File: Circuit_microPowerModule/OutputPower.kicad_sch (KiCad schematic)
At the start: 31 parts, among them U4 LM358, U7 MP2315S, U8 LM358

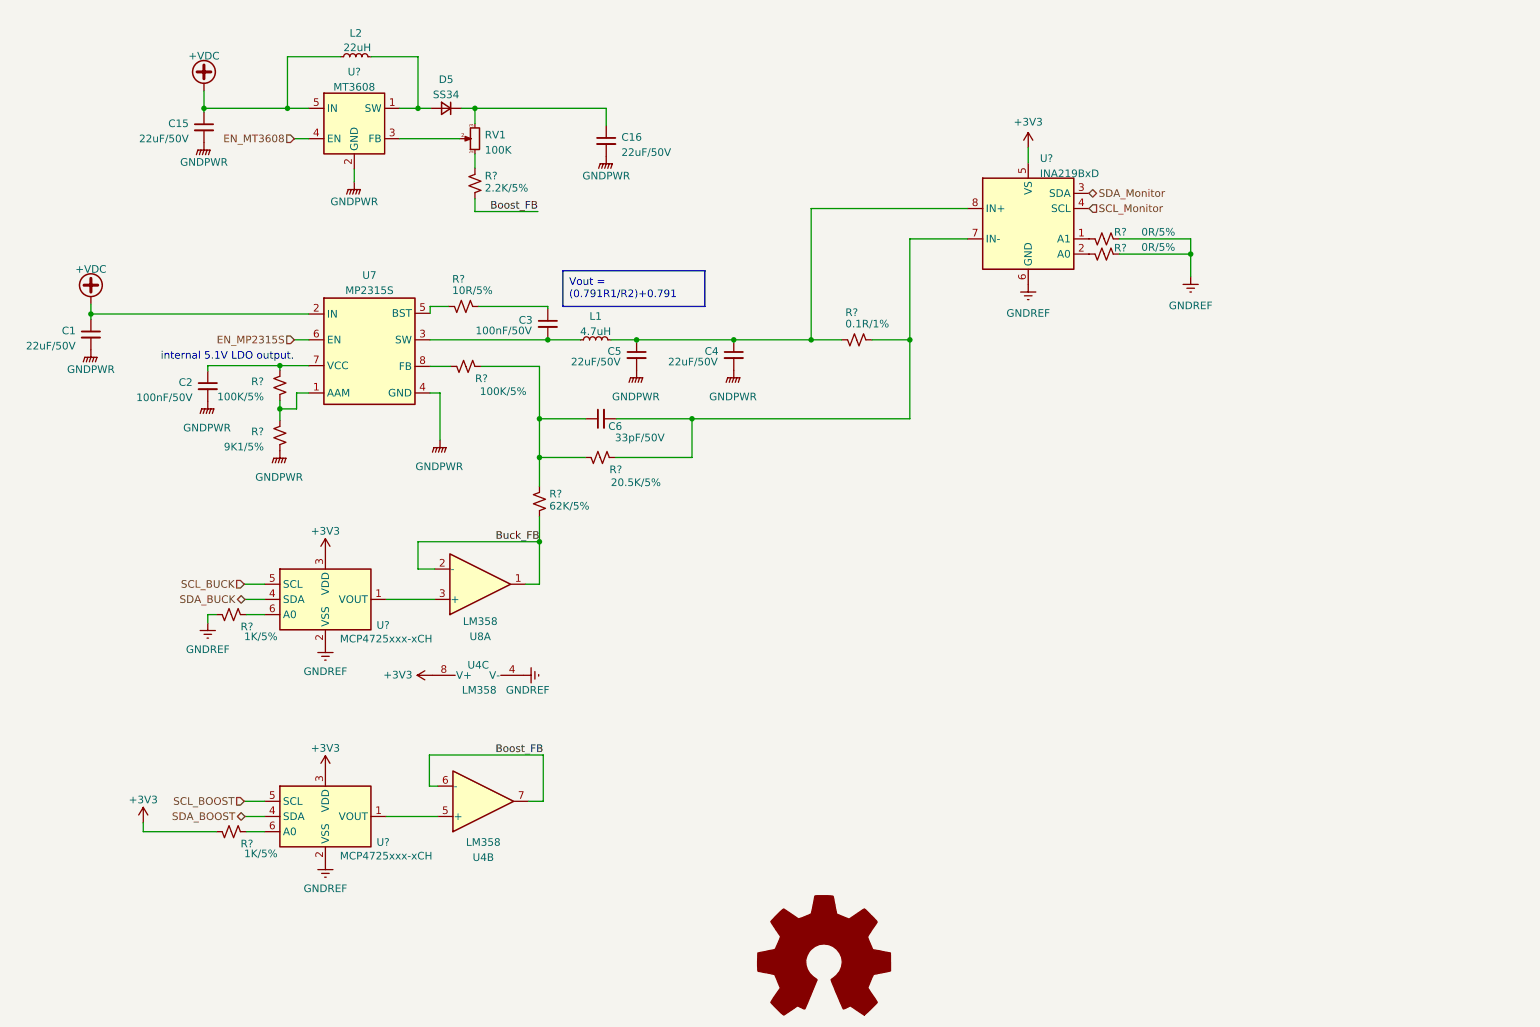
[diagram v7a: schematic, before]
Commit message: update schematic
added pin assessment to readme
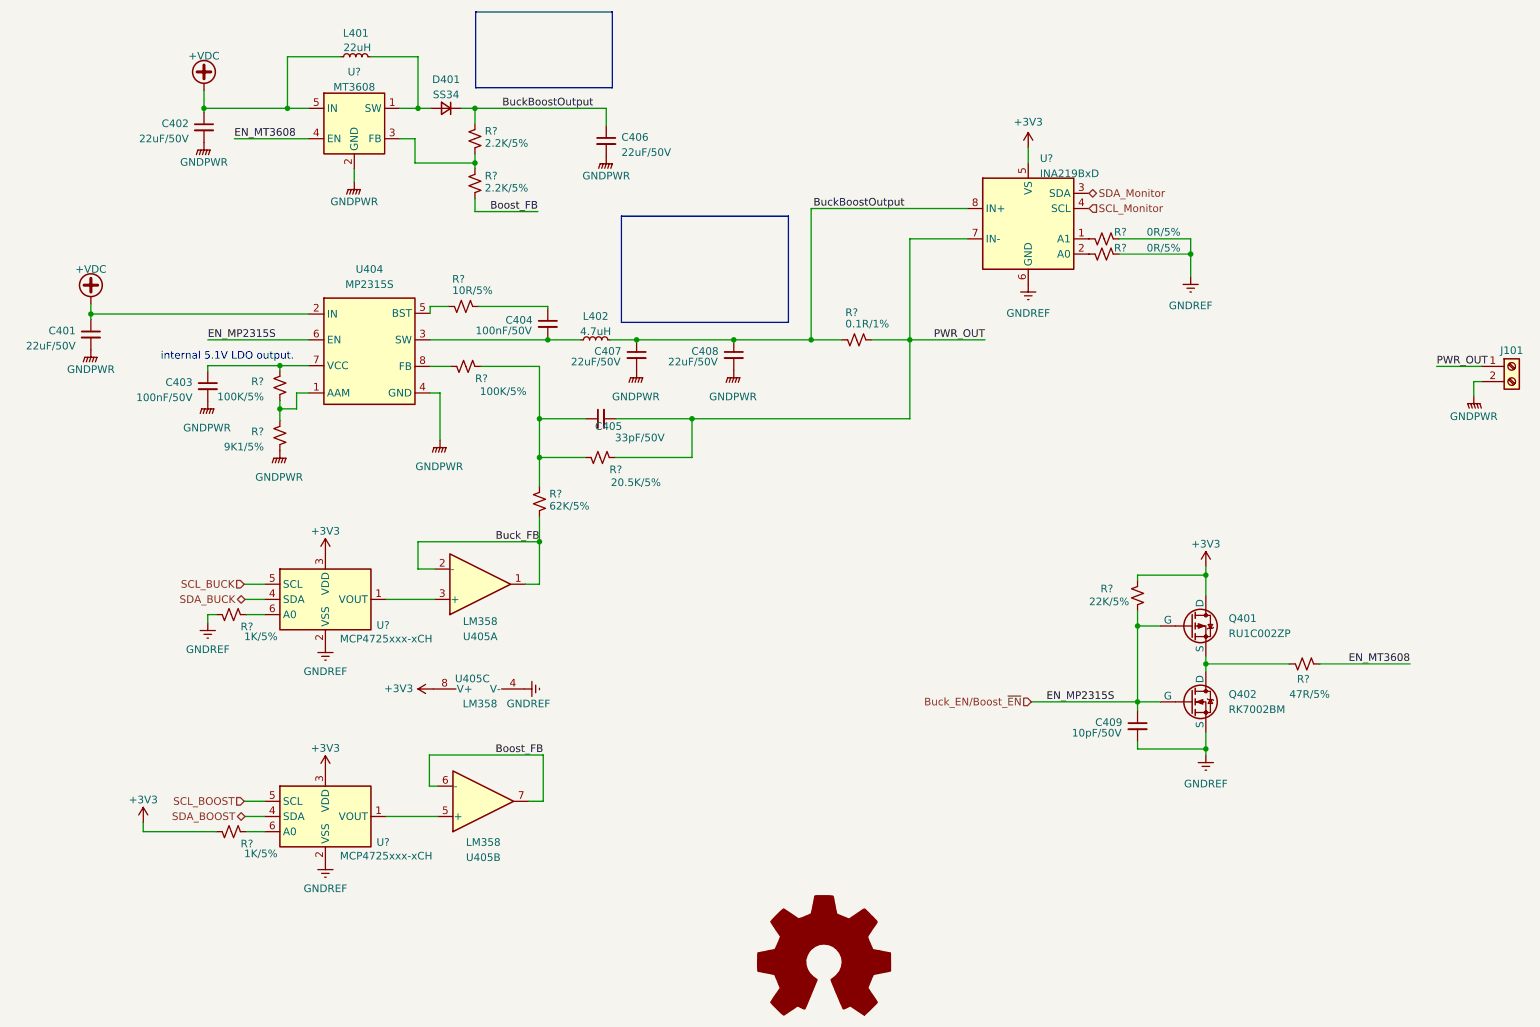
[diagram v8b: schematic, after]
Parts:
- removed RV1: 100K, symbol Device:R_Potentiometer_Small
- added C409: 10pF/50V, symbol Device:C_Small
- added J101: Screw_Terminal_01x02, Connector_Phoenix_MC:PhoenixContact_MC_1,5_2-G-3.81_1x02_P3.81mm_Horizontal, symbol Connector:Screw_Terminal_01x02
- added Q401: RU1C002ZP, symbol Simulation_SPICE:PMOS
- added Q402: RK7002BM, symbol Simulation_SPICE:NMOS
- added R?: 22K/5%, Resistor_SMD:R_0603_1608Metric, symbol Device:R_Small_US
- added R?: 47R/5%, Resistor_SMD:R_0603_1608Metric, symbol Device:R_Small_US
- added R?: 2.2K/5%, Resistor_SMD:R_0603_1608Metric, symbol Device:R_Small_US
- renumbered C1 to C401, C15 to C402, C2 to C403, C3 to C404, C6 to C405, C16 to C406, C5 to C407, C4 to C408, D5 to D401, L2 to L401, L1 to L402, U7 to U404, U8 to U405, U4 to U405
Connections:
- net +3V3: now also Q401.1 (D), R?.2
- net EN_MT3608: now also R?.2
- net GNDPWR: now also J101.2 (Pin_2)
- net GNDREF: now also C409.2, Q402.3 (S)
- net PWR_OUT: now reaches C405.2, R?.1, R?.2, U?.7 (IN-)
- net PWR_OUT: now also J101.1 (Pin_1)
- net BuckBoostOutput: now reaches C407.1, C408.1, L402.2, R?.1, U?.8 (IN+)
- net BuckBoostOutput: now also C406.1, D401.1 (K), R?.1
- net at R?.1: now also U?.3 (FB), R?.2
- net EN_MP2315S renamed Buck_EN/Boost_~{EN}
- net Buck_EN/Boost_~{EN}: now also C409.1, Q401.2 (G), Q402.2 (G), R?.1
- new net: Q401.3 (S), Q402.1 (D), R?.1
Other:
- moved on the sheet: U405C
